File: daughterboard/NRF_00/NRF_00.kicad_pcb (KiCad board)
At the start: 4 copper layers, 67 x 50 mm, 2 parts, among them J1 m2_keyA_67pin_daughterboard

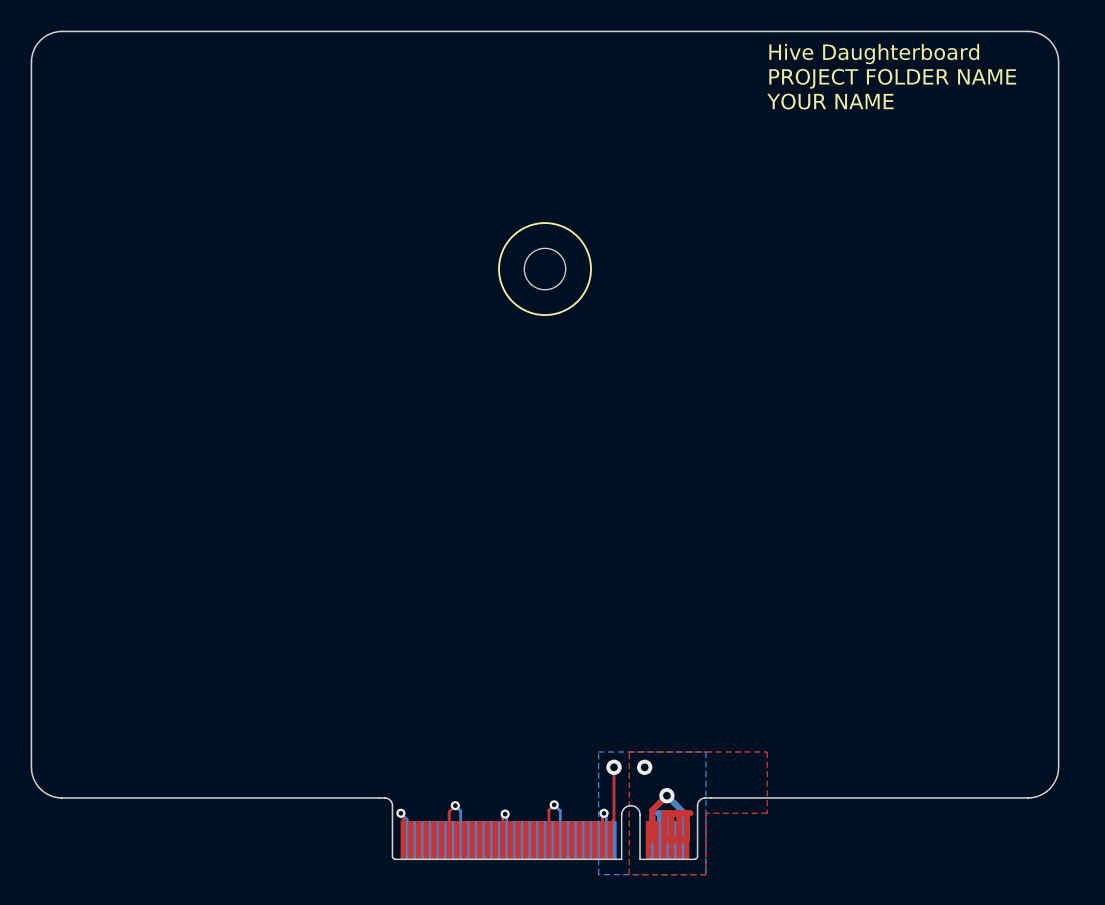
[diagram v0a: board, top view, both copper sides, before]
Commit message: finished NRF daughterboard layout
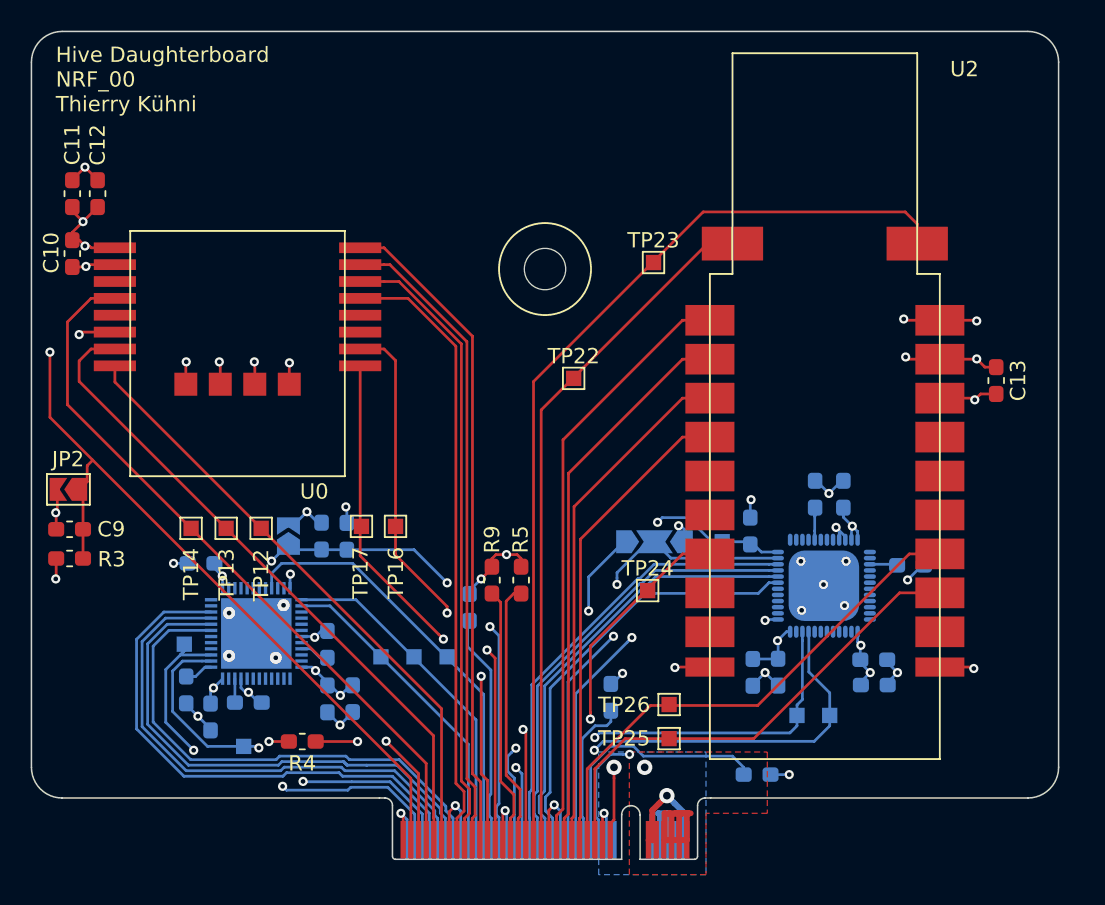
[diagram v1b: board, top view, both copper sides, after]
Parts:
- added C1: 100n, Capacitor_SMD:C_0603_1608Metric_Pad1.05x0.95mm_HandSolder, B.Cu at (133.9, 109.9)
- added C10: 100n, Capacitor_SMD:C_0603_1608Metric_Pad1.05x0.95mm_HandSolder, F.Cu at (117.7, 91.5)
- added C11: 4.7u, Capacitor_SMD:C_0603_1608Metric_Pad1.05x0.95mm_HandSolder, F.Cu at (117.7, 87.6)
- added C12: 10u, Capacitor_SMD:C_0603_1608Metric_Pad1.05x0.95mm_HandSolder, F.Cu at (119.3, 87.6)
- added C13: 10u, Capacitor_SMD:C_0603_1608Metric_Pad1.05x0.95mm_HandSolder, F.Cu at (177.9, 99.8)
- added C14: 100n, Capacitor_SMD:C_0603_1608Metric_Pad1.05x0.95mm_HandSolder, B.Cu at (168.0, 107.2)
- added C15: 100n, Capacitor_SMD:C_0603_1608Metric_Pad1.05x0.95mm_HandSolder, B.Cu at (172.3, 111.8)
- added C16: 100n, Capacitor_SMD:C_0603_1608Metric_Pad1.05x0.95mm_HandSolder, B.Cu at (166.1, 107.2)
- added C17: 100n, Capacitor_SMD:C_0603_1608Metric_Pad1.05x0.95mm_HandSolder, B.Cu at (163.7, 118.8)
- added C18: 100n, Capacitor_SMD:C_0603_1608Metric_Pad1.05x0.95mm_HandSolder, B.Cu at (162.1, 118.8)
- added C19: 100n, Capacitor_SMD:C_0603_1608Metric_Pad1.05x0.95mm_HandSolder, B.Cu at (169.9, 118.0)
- added C2: 100n, Capacitor_SMD:C_0603_1608Metric_Pad1.05x0.95mm_HandSolder, B.Cu at (126.7, 121.7)
- added C20: 4.7u, Capacitor_SMD:C_0603_1608Metric_Pad1.05x0.95mm_HandSolder, B.Cu at (170.0, 119.6)
- added C3: 100n, Capacitor_SMD:C_0603_1608Metric_Pad1.05x0.95mm_HandSolder, B.Cu at (134.3, 120.5)
- added C4: 100n, Capacitor_SMD:C_0603_1608Metric_Pad1.05x0.95mm_HandSolder, B.Cu at (126.1, 111.7)
- added C5: 4.7u, Capacitor_SMD:C_0603_1608Metric_Pad1.05x0.95mm_HandSolder, B.Cu at (136.0, 120.5)
- added C6: 1u, Capacitor_SMD:C_0603_1608Metric_Pad1.05x0.95mm_HandSolder, B.Cu at (129.1, 120.8)
- added C7: 100p, Capacitor_SMD:C_0603_1608Metric_Pad1.05x0.95mm_HandSolder, B.Cu at (134.3, 117.0)
- added C8: 100n, Capacitor_SMD:C_0603_1608Metric_Pad1.05x0.95mm_HandSolder, B.Cu at (125.1, 120.0)
- added C9: 100n, Capacitor_SMD:C_0603_1608Metric_Pad1.05x0.95mm_HandSolder, F.Cu at (117.5, 109.5)
- added JP1: NRST, Jumper:SolderJumper-2_P1.3mm_Open_TrianglePad1.0x1.5mm, B.Cu at (131.8, 109.9)
- added JP2: NRST, Jumper:SolderJumper-2_P1.3mm_Open_TrianglePad1.0x1.5mm, F.Cu at (117.4, 106.9)
- added JP3: NRST_DEBUG, Jumper:SolderJumper-3_P2.0mm_Open_TrianglePad1.0x1.5mm_NumberLabels, B.Cu at (155.6, 110.3)
- added R1: 100k, Resistor_SMD:R_0603_1608Metric_Pad1.05x0.95mm_HandSolder, B.Cu at (135.6, 109.9)
- added R2: 100k, Resistor_SMD:R_0603_1608Metric_Pad1.05x0.95mm_HandSolder, B.Cu at (143.6, 114.6)
- added R3: 100k, Resistor_SMD:R_0603_1608Metric_Pad1.05x0.95mm_HandSolder, F.Cu at (117.5, 111.4)
- added R4: 100k, Resistor_SMD:R_0603_1608Metric_Pad1.05x0.95mm_HandSolder, F.Cu at (132.7, 123.3)
- added R5: 100k, Resistor_SMD:R_0603_1608Metric_Pad1.05x0.95mm_HandSolder, F.Cu at (146.9, 112.8)
- added R6: 1k, Resistor_SMD:R_0603_1608Metric_Pad1.05x0.95mm_HandSolder, B.Cu at (161.9, 109.6)
- added R7: 100k, Resistor_SMD:R_0603_1608Metric_Pad1.05x0.95mm_HandSolder, B.Cu at (162.3, 125.5)
- added R8: 100k, Resistor_SMD:R_0603_1608Metric_Pad1.05x0.95mm_HandSolder, B.Cu at (152.8, 120.4)
- added R9: 100k, Resistor_SMD:R_0603_1608Metric_Pad1.05x0.95mm_HandSolder, F.Cu at (145.0, 112.8)
- added TP12: SWDIO, TestPoint:TestPoint_Pad_1.0x1.0mm, F.Cu at (130.0, 109.4)
- added TP13: SWDCLK, TestPoint:TestPoint_Pad_1.0x1.0mm, F.Cu at (127.7, 109.4)
- added TP14: SWO, TestPoint:TestPoint_Pad_1.0x1.0mm, F.Cu at (125.4, 109.4)
- added TP16: UART_TX, TestPoint:TestPoint_Pad_1.0x1.0mm, F.Cu at (138.7, 109.3)
- added TP17: UART_RX, TestPoint:TestPoint_Pad_1.0x1.0mm, F.Cu at (136.5, 109.3)
- added TP2: SWDIO, TestPoint:TestPoint_Pad_1.0x1.0mm, B.Cu at (137.8, 117.8)
- added TP22: SWDIO, TestPoint:TestPoint_Pad_1.0x1.0mm, F.Cu at (150.4, 99.6)
- added TP23: SWDCLK, TestPoint:TestPoint_Pad_1.0x1.0mm, F.Cu at (155.6, 92.1)
- added TP24: SWO, TestPoint:TestPoint_Pad_1.0x1.0mm, F.Cu at (155.2, 113.5)
- added TP25: UART_TX, TestPoint:TestPoint_Pad_1.0x1.0mm, F.Cu at (156.6, 123.1)
- added TP26: UART_RX, TestPoint:TestPoint_Pad_1.0x1.0mm, F.Cu at (156.6, 120.9)
- added TP3: SWDCLK, TestPoint:TestPoint_Pad_1.0x1.0mm, B.Cu at (140.0, 117.8)
- added TP32: SWDCLK, TestPoint:TestPoint_Pad_1.0x1.0mm, B.Cu at (160.1, 110.3)
- added TP35: UART_TX, TestPoint:TestPoint_Pad_1.0x1.0mm, B.Cu at (164.9, 121.6)
- added TP36: UART_RX, TestPoint:TestPoint_Pad_1.0x1.0mm, B.Cu at (167.1, 121.6)
- added TP4: SWO, TestPoint:TestPoint_Pad_1.0x1.0mm, B.Cu at (142.1, 117.8)
- added TP6: UART_TX, TestPoint:TestPoint_Pad_1.0x1.0mm, B.Cu at (125.0, 117.0)
- added TP7: UART_RX, TestPoint:TestPoint_Pad_1.0x1.0mm, B.Cu at (128.8, 123.6)
- added U0: BT40E, hive_daughterboard:BT40E, F.Cu at (128.4, 90.0)
- added U1: nRF52832-QFAB-T, hive_daughterboard:nRF52832-QFAB-T, B.Cu at (129.7, 116.3)
- added U2: NRF52840-USB-DONGLE, hive_daughterboard:NRF52840-USB-DONGLE, F.Cu at (166.8, 124.5)
- added U3: NRF51822-QFAC-R7, hive_daughterboard:NRF51822-QFAC-R7, B.Cu at (166.7, 113.2)
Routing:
- net /Target 2/TCK|SWDCLK_2: track 0.00 -> 61.1 mm
- net GND: track 28.1 -> 86.4 mm, vias 6 -> 44
- net /Target 0/RST_0: track 0.00 -> 53.2 mm, vias 0 -> 2
- net /Target 0/TDO|SWO_0: track 0.00 -> 47.2 mm
- net /Target 2/TMS|SWDIO_2: track 0.00 -> 45.0 mm
- net /Target 0/TCK|SWDCLK_0: track 0.00 -> 43.5 mm
- net /Target 0/GPIO0.3: track 0.00 -> 42.8 mm
- net /Target 0/GPIO0.2: track 0.00 -> 41.9 mm
- net /Target 0/GPIO0.1: track 0.00 -> 41.0 mm
- net +3V3: track 11.6 -> 51.7 mm, vias 2 -> 18
- net /Target 0/GPIO0.0: track 0.00 -> 40.2 mm
- net /Target 0/TMS|SWDIO_0: track 0.00 -> 39.8 mm
- net /Target 2/GPIO2.0: track 0.00 -> 39.1 mm
- net /Target 0/UART_RxD0: track 0.00 -> 36.7 mm, vias 0 -> 2
- net /Target 2/GPIO2.1: track 0.00 -> 36.3 mm
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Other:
- net class Signal: clearance 0.18 -> 0.14
- board text added: "Hive Daughterboard NRF_00 Thierry Kühni"
- board text removed: "Hive Daughterboard PROJECT FOLDER NAME YOUR NAME"

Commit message: length matching daughterboards
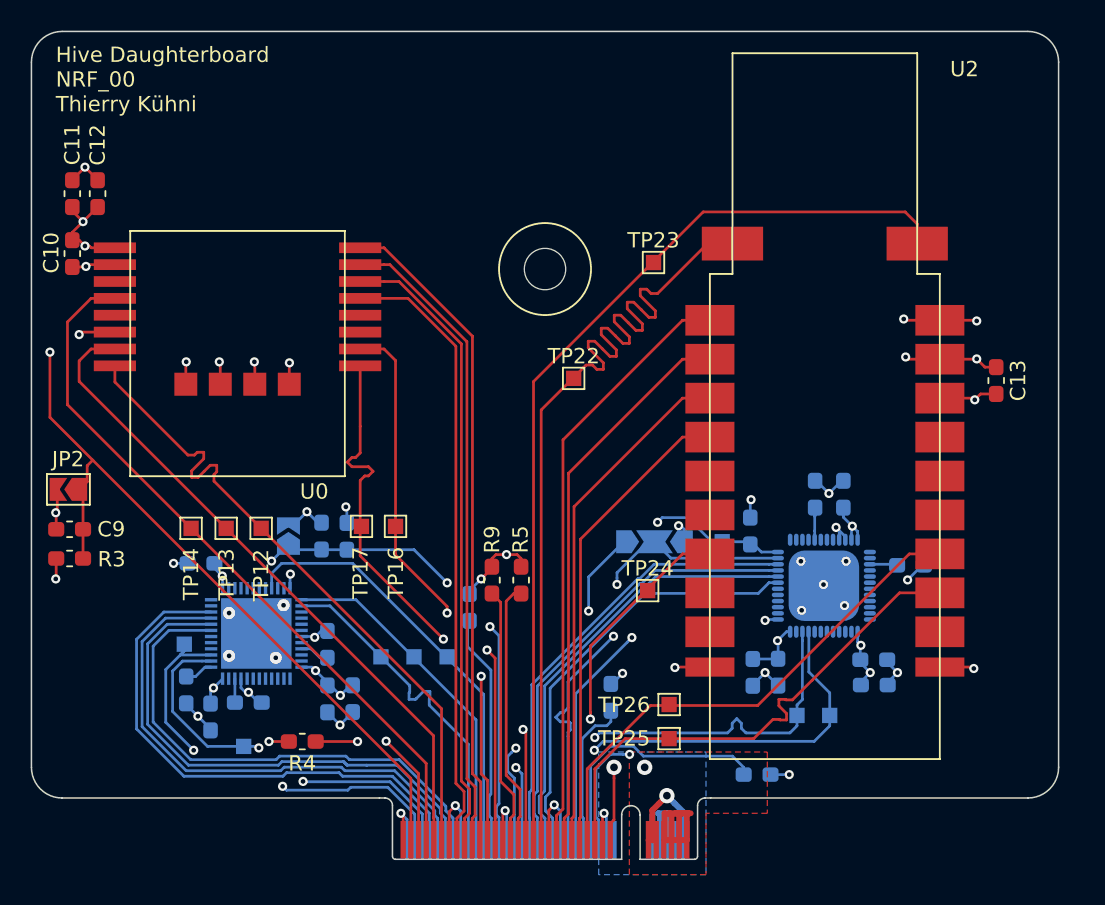
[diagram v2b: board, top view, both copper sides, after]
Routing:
- net /Target 2/TMS|SWDIO_2: track 45.0 -> 61.1 mm
- net /Target 0/TMS|SWDIO_0: track 39.8 -> 43.5 mm
- net /Target 0/UART_TxD0: track 34.4 -> 36.7 mm
- net /Target 1/UART_TxD1: track 26.2 -> 28.0 mm
- net /Target 1/TMS|SWDIO_1: track 20.9 -> 22.5 mm
- net /Target 2/UART_RxD2: track 31.9 -> 33.5 mm
- net /Target 3/TMS|SWDIO_3: track 30.5 -> 31.8 mm
- net /Target 3/UART_RxD3: track 31.6 -> 32.8 mm
